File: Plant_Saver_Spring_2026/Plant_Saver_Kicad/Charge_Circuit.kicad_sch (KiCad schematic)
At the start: 23 parts, among them J1 1.25mm, Q1 ISP12DP06NMXTSA1, Q2 G09P02L, Q3 G09P02L, Q4 G09P02L, Q5 G09P02L, Q6 G09P02L, Q7 G09P02L, Q8 G09P02L, SW7 SA72SB0, U10 DW03C, U11 CDBA140SL-HF, U12 CDBA140SL-HF

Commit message: Found NTC Thermistor
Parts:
- R4, R5: value Therm -> NTCLE317E4103SBA
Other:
- moved on the sheet: BT1, C3, J1, Q1, Q2, Q3, Q4, Q5, Q6, Q7, Q8, R2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

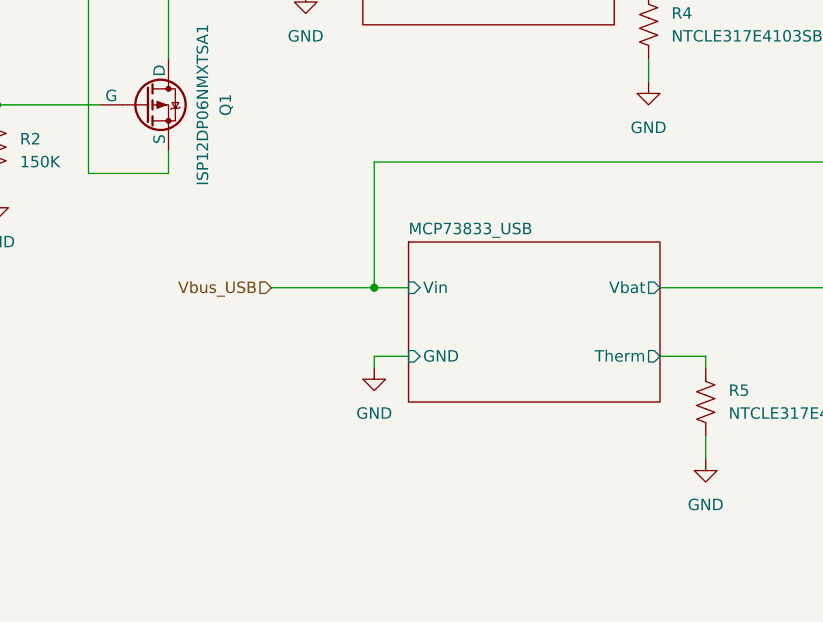
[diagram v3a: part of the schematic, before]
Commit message: Footprint updates
Misc. schematic fixes, mostly updated/added footprints where needed.
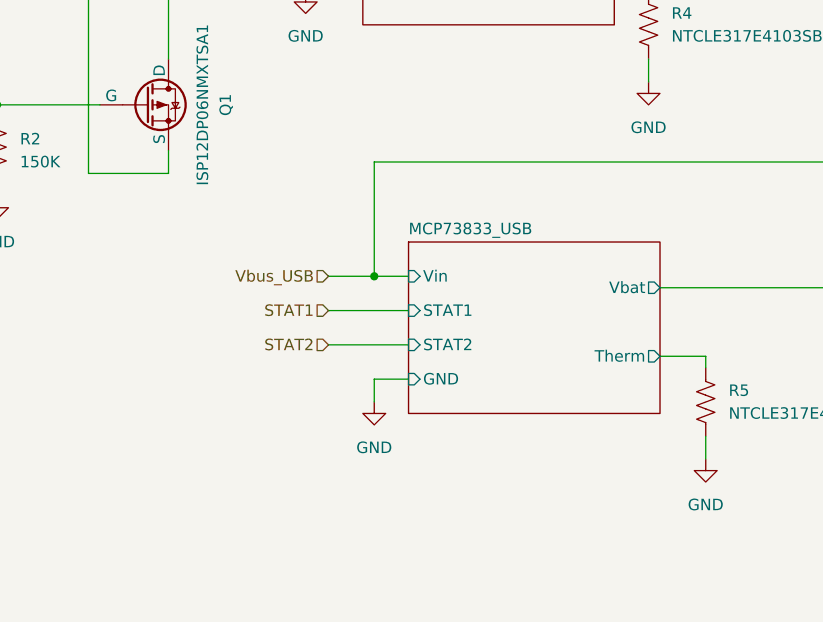
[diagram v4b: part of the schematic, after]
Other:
- sheet MCP73833_USB ports: added STAT1, STAT2; removed none
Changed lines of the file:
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@@
 	)
 	(junction
-		(at 113.03 87.63)
-		(diameter 0)
-		(color 0 0 0 0)
-	)
-	(junction
 		(at 166.37 73.66)
 		(diameter 0)
@@
 	)
 	(junction
+		(at 113.03 86.36)
+		(diameter 0)
+		(color 0 0 0 0)
+	)
+	(junction
 		(at 172.72 54.61)
 		(diameter 0)
@@
 	(wire
 		(pts
-			(xy 116.84 95.25) (xy 113.03 95.25)
+			(xy 113.03 86.36) (xy 116.84 86.36)
 		)
 		(stroke
@@
 	(wire
 		(pts
-			(xy 113.03 87.63) (xy 116.84 87.63)
+			(xy 139.7 45.72) (xy 154.94 45.72)
 		)
 		(stroke
@@
 	(wire
 		(pts
-			(xy 139.7 45.72) (xy 154.94 45.72)
+			(xy 107.95 86.36) (xy 113.03 86.36)
 		)
 		(stroke
@@
 	(wire
 		(pts
-			(xy 101.6 87.63) (xy 113.03 87.63)
+			(xy 39.37 50.8) (xy 39.37 52.07)
 		)
 		(stroke
@@
 	(wire
 		(pts
-			(xy 39.37 50.8) (xy 39.37 52.07)
+			(xy 238.76 95.25) (xy 234.95 95.25)
 		)
 		(stroke
@@
 	(wire
 		(pts
-			(xy 238.76 95.25) (xy 234.95 95.25)
+			(xy 201.93 78.74) (xy 203.2 78.74)
 		)
 		(stroke
@@
 	(wire
 		(pts
-			(xy 201.93 78.74) (xy 203.2 78.74)
+			(xy 210.82 80.01) (xy 210.82 78.74)
 		)
 		(stroke
@@
 	(wire
 		(pts
-			(xy 210.82 80.01) (xy 210.82 78.74)
+			(xy 166.37 73.66) (xy 166.37 54.61)
 		)
 		(stroke
@@
 	(wire
 		(pts
-			(xy 166.37 73.66) (xy 166.37 54.61)
+			(xy 107.95 93.98) (xy 116.84 93.98)
 		)
 		(stroke
@@
 	(wire
 		(pts
-			(xy 113.03 95.25) (xy 113.03 96.52)
+			(xy 107.95 45.72) (xy 107.95 35.56)
 		)
 		(stroke
@@
 	(wire
 		(pts
-			(xy 107.95 45.72) (xy 107.95 35.56)
+			(xy 143.51 62.23) (xy 143.51 64.77)
 		)
 		(stroke
@@
 	(wire
 		(pts
-			(xy 143.51 62.23) (xy 143.51 64.77)
+			(xy 213.36 60.96) (xy 218.44 60.96)
 		)
 		(stroke
@@
 	(wire
 		(pts
-			(xy 213.36 60.96) (xy 218.44 60.96)
+			(xy 113.03 97.79) (xy 113.03 100.33)
 		)
 		(stroke
@@
 	(wire
 		(pts
-			(xy 113.03 87.63) (xy 113.03 73.66)
+			(xy 185.42 43.18) (xy 185.42 44.45)
 		)
 		(stroke
@@
 	(wire
 		(pts
-			(xy 185.42 43.18) (xy 185.42 44.45)
+			(xy 210.82 132.08) (xy 210.82 135.89)
 		)
 		(stroke
@@
 	(wire
 		(pts
-			(xy 210.82 132.08) (xy 210.82 135.89)
+			(xy 113.03 86.36) (xy 113.03 73.66)
 		)
 		(stroke
@@
 	(wire
 		(pts
+			(xy 107.95 90.17) (xy 116.84 90.17)
+		)
+		(stroke
+			(width 0)
+			(type default)
+		)
+	)
+	(wire
+		(pts
 			(xy 223.52 60.96) (xy 218.44 60.96)
 		)
@@
 	(wire
 		(pts
+			(xy 113.03 97.79) (xy 116.84 97.79)
+		)
+		(stroke
+			(width 0)
+			(type default)
+		)
+	)
+	(wire
+		(pts
 			(xy 210.82 135.89) (xy 207.01 135.89)
 		)
@@
 		)
 	)
+	(hierarchical_label "STAT2"
+		(shape input)
+		(at 107.95 93.98 180)
+		(effects
+			(font
+				(size 1.27 1.27)
+			)
+			(justify right)
+		)
+	)
+	(hierarchical_label "STAT1"
+		(shape input)
+		(at 107.95 90.17 180)
+		(effects
+			(font
+				(size 1.27 1.27)
+			)
+			(justify right)
+		)
+	)
 	(hierarchical_label "3V3"
 		(shape input)
@@
 	(hierarchical_label "Vbus_USB"
 		(shape input)
-		(at 101.6 87.63 180)
+		(at 107.95 86.36 180)
 		(effects
 			(font
@@
 	(symbol
 		(lib_id "power:GND")
-		(at 113.03 96.52 0)
+		(at 113.03 100.33 0)
 		(unit 1)
 		(exclude_from_sim no)
@@
 		(fields_autoplaced yes)
 		(property "Reference" "#PWR016"
-			(at 113.03 102.87 0)
+			(at 113.03 106.68 0)
 			(effects
 				(font
@@
 		)
 		(property "Value" "GND"
-			(at 113.03 101.6 0)
+			(at 113.03 105.41 0)
 			(effects
 				(font
@@
 		)
 		(property "Footprint" ""
-			(at 113.03 96.52 0)
+			(at 113.03 100.33 0)
 			(effects
 				(font
@@
 		)
 		(property "Datasheet" ""
-			(at 113.03 96.52 0)
+			(at 113.03 100.33 0)
 			(effects
 				(font
@@
 		)
 		(property "Description" "Power symbol creates a global label with name \"GND\" , ground"
-			(at 113.03 96.52 0)
+			(at 113.03 100.33 0)
 			(effects
 				(font
@@
 	(sheet
 		(at 116.84 82.55)
-		(size 27.94 17.78)
+		(size 27.94 19.05)
 		(exclude_from_sim no)
 		(in_bom yes)
@@
 		)
 		(property "Sheetfile" "MCP73833_USB.kicad_sch"
-			(at 116.84 100.9146 0)
+			(at 116.84 102.1846 0)
 			(effects
 				(font
@@
 		)
 		(pin "GND" input
-			(at 116.84 95.25 180)
+			(at 116.84 97.79 180)
 			(effects
 				(font
@@
 		)
 		(pin "Vin" input
-			(at 116.84 87.63 180)
+			(at 116.84 86.36 180)
+			(effects
+				(font
+					(size 1.27 1.27)
+				)
+				(justify left)
+			)
+		)
+		(pin "STAT1" input
+			(at 116.84 90.17 180)
+			(effects
+				(font
+					(size 1.27 1.27)
+				)
+				(justify left)
+			)
+		)
+		(pin "STAT2" input
+			(at 116.84 93.98 180)
 			(effects
 				(font

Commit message: Started PCB
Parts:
- added TP10, TP8, TP9: TestPoint, TestPoint:TestPoint_Pad_1.5x1.5mm, symbol Connector:TestPoint
- U10: footprint (none) -> Package_TO_SOT_SMD:SOT-23-5_HandSoldering
- U11: renamed from U12; footprint (none) -> CDBA140SL_HF:CDBA-HF
- U9: renamed from U11; footprint (none) -> CDBA140SL_HF:CDBA-HF
- renumbered C3 to C5, J1 to J9, Q8 to Q10, Q1 to Q3, Q2 to Q4, Q3 to Q5, Q4 to Q6, Q5 to Q7, Q6 to Q8, Q7 to Q9, R5 to R10, R6 to R11, R8 to R12, R9 to R13, R7 to R14, R2 to R7, R3 to R8, R4 to R9, SW7 to SW4
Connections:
- net MCP73833_Solar/Vin: now also TP8.1
- net MCP73833_USB/Vbat: now also TP9.1
- net Vout: now also TP10.1

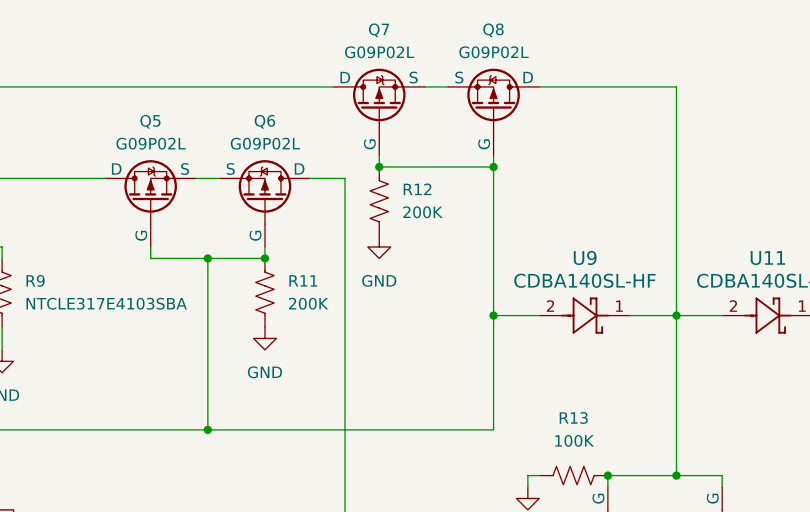
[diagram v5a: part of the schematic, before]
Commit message: Refined PCB layout
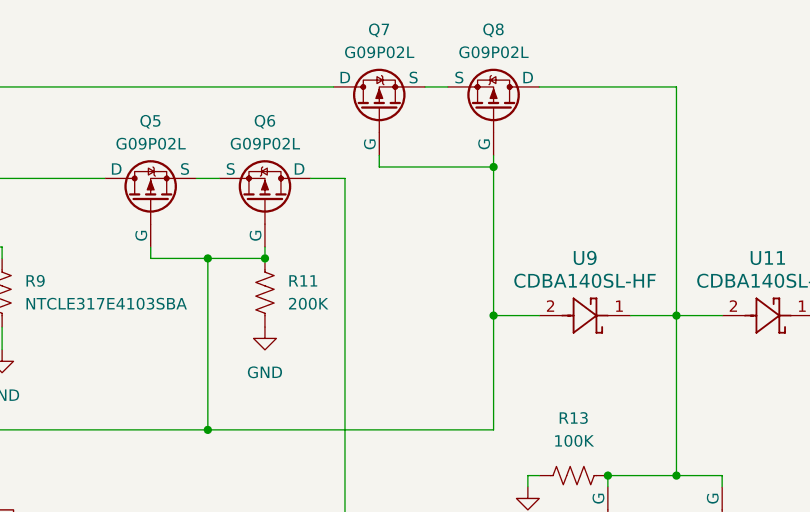
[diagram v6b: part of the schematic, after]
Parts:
- removed R12: 200K, Resistor_THT:R_Axial_DIN0207_L6.3mm_D2.5mm_P10.16mm_Horizontal, symbol Device:R_US
- C5: footprint C410C105K5R5TA7200:CAP_C410C_AX_X7R_AXIMAX_KEM -> Capacitor_SMD:C_1206_3216Metric_Pad1.33x1.80mm_HandSolder
- R11, R13, R14, R7, R8: footprint Resistor_THT:R_Axial_DIN0207_L6.3mm_D2.5mm_P10.16mm_Horizontal -> Resistor_SMD:R_1206_3216Metric_Pad1.30x1.75mm_HandSolder
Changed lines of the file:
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@@
 	)
 	(junction
-		(at 185.42 44.45)
-		(diameter 0)
-		(color 0 0 0 0)
-	)
-	(junction
 		(at 210.82 116.84)
 		(diameter 0)
@@
 	(symbol
 		(lib_id "Device:R_US")
-		(at 185.42 48.26 180)
-		(unit 1)
-		(exclude_from_sim no)
-		(in_bom yes)
-		(on_board yes)
-		(dnp no)
-		(fields_autoplaced yes)
-		(property "Reference" "R12"
-			(at 187.96 46.9899 0)
-			(effects
-				(font
-					(size 1.27 1.27)
-				)
-				(justify right)
-			)
-		)
-		(property "Value" "200K"
-			(at 187.96 49.5299 0)
-			(effects
-				(font
-					(size 1.27 1.27)
-				)
-				(justify right)
-			)
-		)
-		(property "Footprint" "Resistor_THT:R_Axial_DIN0207_L6.3mm_D2.5mm_P10.16mm_Horizontal"
-			(at 184.404 48.006 90)
-			(effects
-				(font
-					(size 1.27 1.27)
-				)
-				(hide yes)
-			)
-		)
-		(property "Datasheet" "~"
-			(at 185.42 48.26 0)
-			(effects
-				(font
-					(size 1.27 1.27)
-				)
-				(hide yes)
-			)
-		)
-		(property "Description" "Resistor, US symbol"
-			(at 185.42 48.26 0)
-			(effects
-				(font
-					(size 1.27 1.27)
-				)
-				(hide yes)
-			)
-		)
-		(pin "2"
-		)
-		(pin "1"
-		)
-		(instances
-			(project "Plant_Saver_Dev"
-				(path "/681e180a-075d-4ade-9671-1538248e0c71/5dcd62e6-4375-4774-94ca-6833cc877f09"
-					(reference "R15")
-					(unit 1)
-				)
-			)
-			(project "Charge_Circuit"
-				(path "/6972ab9f-ec90-4565-bd2c-bfb60d5a21f0"
-					(reference "R7")
-					(unit 1)
-				)
-			)
-			(project "Plant_Saver_Dev"
-				(path "/7f244634-d37a-4ff0-ba36-8027330ab1bd/c1b5c94f-5fb5-4e2b-895b-5d171c372d7d"
-					(reference "R12")
-					(unit 1)
-				)
-			)
-		)
-	)
-	(symbol
-		(lib_id "Device:R_US")
 		(at 172.72 58.42 180)
 		(unit 1)
@@
 			)
 		)
-		(property "Footprint" "Resistor_THT:R_Axial_DIN0207_L6.3mm_D2.5mm_P10.16mm_Horizontal"
+		(property "Footprint" "Resistor_SMD:R_1206_3216Metric_Pad1.30x1.75mm_HandSolder"
 			(at 171.704 58.166 90)
 			(effects
@@
 			)
 		)
-		(property "Footprint" "Resistor_THT:R_Axial_DIN0207_L6.3mm_D2.5mm_P10.16mm_Horizontal"
+		(property "Footprint" "Resistor_SMD:R_1206_3216Metric_Pad1.30x1.75mm_HandSolder"
 			(at 70.104 72.136 90)
 			(effects
@@
 			)
 		)
-		(property "Footprint" "Resistor_THT:R_Axial_DIN0207_L6.3mm_D2.5mm_P10.16mm_Horizontal"
+		(property "Footprint" "Resistor_SMD:R_1206_3216Metric_Pad1.30x1.75mm_HandSolder"
 			(at 206.756 79.756 90)
 			(effects
@@
 			)
 		)
-		(property "Footprint" "Resistor_THT:R_Axial_DIN0207_L6.3mm_D2.5mm_P10.16mm_Horizontal"
+		(property "Footprint" "Resistor_SMD:R_1206_3216Metric_Pad1.30x1.75mm_HandSolder"
 			(at 207.264 105.664 90)
 			(effects
@@
 			)
 		)
-		(property "Footprint" "C410C105K5R5TA7200:CAP_C410C_AX_X7R_AXIMAX_KEM"
+		(property "Footprint" "Capacitor_SMD:C_1206_3216Metric_Pad1.33x1.80mm_HandSolder"
 			(at 209.55 115.8748 0)
 			(effects
@@
 			)
 		)
-		(property "Footprint" "Resistor_THT:R_Axial_DIN0207_L6.3mm_D2.5mm_P10.16mm_Horizontal"
+		(property "Footprint" "Resistor_SMD:R_1206_3216Metric_Pad1.30x1.75mm_HandSolder"
 			(at 98.044 52.324 90)
 			(effects
@@
 					(unit 1)
 				)
-			)
-		)
-	)
-	(symbol
-		(lib_id "power:GND")
-		(at 185.42 52.07 0)
-		(unit 1)
-		(exclude_from_sim no)
-		(in_bom yes)
-		(on_board yes)
-		(dnp no)
-		(fields_autoplaced yes)
-		(property "Reference" "#PWR022"
-			(at 185.42 58.42 0)
-			(effects
-				(font
-					(size 1.27 1.27)
-				)
-				(hide yes)
-			)
-		)
-		(property "Value" "GND"
-			(at 185.42 57.15 0)
-			(effects
-				(font
-					(size 1.27 1.27)
-				)
-			)
-		)
-		(property "Footprint" ""
-			(at 185.42 52.07 0)
-			(effects
-				(font
-					(size 1.27 1.27)
-				)
-				(hide yes)
-			)
-		)
-		(property "Datasheet" ""
-			(at 185.42 52.07 0)
-			(effects
-				(font
-					(size 1.27 1.27)
-				)
-				(hide yes)
-			)
-		)
-		(property "Description" "Power symbol creates a global label with name \"GND\" , ground"
-			(at 185.42 52.07 0)
-			(effects
-				(font
-					(size 1.27 1.27)
-				)
-				(hide yes)
-			)
-		)
-		(pin "1"
-		)
-		(instances
-			(project "Plant_Saver_Dev"
-				(path "/681e180a-075d-4ade-9671-1538248e0c71/5dcd62e6-4375-4774-94ca-6833cc877f09"
-					(reference "#PWR04")
-					(unit 1)
-				)
-			)
-			(project "Charge_Circuit"
-				(path "/6972ab9f-ec90-4565-bd2c-bfb60d5a21f0"
-					(reference "#PWR09")
-					(unit 1)
-				)
-			)
-			(project "Plant_Saver_Dev"
-				(path "/7f244634-d37a-4ff0-ba36-8027330ab1bd/c1b5c94f-5fb5-4e2b-895b-5d171c372d7d"
-					(reference "#PWR022")
-					(unit 1)
-				)

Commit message: PCB Routing
I believe this to be the product of mania, but it may yet function.
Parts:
- TP8: footprint TestPoint:TestPoint_Pad_1.5x1.5mm -> TestPoint:TestPoint_Pad_1.0x1.0mm
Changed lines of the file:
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@@
 			)
 		)
-		(property "Footprint" "TestPoint:TestPoint_Pad_1.5x1.5mm"
+		(property "Footprint" "TestPoint:TestPoint_Pad_1.0x1.0mm"
 			(at 104.14 63.5 0)
 			(effects

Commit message: PCB Pre-Check complete
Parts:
- renumbered TP9 to BAT1, TP10 to BUS1, J9 to J10, R8 to R10, R9 to R11, R10 to R12, R11 to R13, R13 to R14, R14 to R15, R7 to R9, TP8 to SOLB1
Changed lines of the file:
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@@
 		(dnp no)
 		(fields_autoplaced yes)
-		(property "Reference" "R11"
+		(property "Reference" "R13"
 			(at 175.26 57.1499 0)
 			(effects
@@
 			(project "Plant_Saver_Dev"
 				(path "/7f244634-d37a-4ff0-ba36-8027330ab1bd/c1b5c94f-5fb5-4e2b-895b-5d171c372d7d"
-					(reference "R11")
+					(reference "R13")
 					(unit 1)
 				)
@@
 		(dnp no)
 		(fields_autoplaced yes)
-		(property "Reference" "TP9"
+		(property "Reference" "BAT1"
 			(at 184.15 94.7419 0)
 			(effects
@@
 			(project "Plant_Saver_Kicad"
 				(path "/7f244634-d37a-4ff0-ba36-8027330ab1bd/c1b5c94f-5fb5-4e2b-895b-5d171c372d7d"
-					(reference "TP9")
+					(reference "BAT1")
 					(unit 1)
 				)
@@
 		(on_board yes)
 		(dnp no)
-		(property "Reference" "J9"
+		(property "Reference" "J10"
 			(at 200.66 143.5099 90)
 			(effects
@@
 			(project ""
 				(path "/7f244634-d37a-4ff0-ba36-8027330ab1bd/c1b5c94f-5fb5-4e2b-895b-5d171c372d7d"
-					(reference "J9")
+					(reference "J10")
 					(unit 1)
 				)
@@
 		(dnp no)
 		(fields_autoplaced yes)
-		(property "Reference" "#PWR018"
+		(property "Reference" "#PWR019"
 			(at 113.03 106.68 0)
 			(effects
@@
 			(project "Plant_Saver_Dev"
 				(path "/7f244634-d37a-4ff0-ba36-8027330ab1bd/c1b5c94f-5fb5-4e2b-895b-5d171c372d7d"
-					(reference "#PWR018")
+					(reference "#PWR019")
 					(unit 1)
 				)
@@
 		(dnp no)
 		(fields_autoplaced yes)
-		(property "Reference" "R7"
+		(property "Reference" "R9"
 			(at 73.66 71.1199 0)
 			(effects
@@
 			(project "Plant_Saver_Dev"
 				(path "/7f244634-d37a-4ff0-ba36-8027330ab1bd/c1b5c94f-5fb5-4e2b-895b-5d171c372d7d"
-					(reference "R7")
+					(reference "R9")
 					(unit 1)
 				)
@@
 		(dnp no)
 		(fields_autoplaced yes)
-		(property "Reference" "R13"
+		(property "Reference" "R14"
 			(at 207.01 72.39 90)
 			(effects
@@
 			(project "Plant_Saver_Dev"
 				(path "/7f244634-d37a-4ff0-ba36-8027330ab1bd/c1b5c94f-5fb5-4e2b-895b-5d171c372d7d"
-					(reference "R13")
+					(reference "R14")
 					(unit 1)
 				)
@@
 		(dnp no)
 		(fields_autoplaced yes)
-		(property "Reference" "R14"
+		(property "Reference" "R15"
 			(at 207.01 100.33 90)
 			(effects
@@
 			(project "Plant_Saver_Kicad"
 				(path "/7f244634-d37a-4ff0-ba36-8027330ab1bd/c1b5c94f-5fb5-4e2b-895b-5d171c372d7d"
-					(reference "R14")
+					(reference "R15")
 					(unit 1)
 				)
@@
 		(on_board yes)
 		(dnp no)
-		(property "Reference" "#PWR019"
+		(property "Reference" "#PWR020"
 			(at 143.51 71.12 0)
 			(effects
@@
 			(project "Plant_Saver_Kicad"
 				(path "/7f244634-d37a-4ff0-ba36-8027330ab1bd/c1b5c94f-5fb5-4e2b-895b-5d171c372d7d"
-					(reference "#PWR019")
+					(reference "#PWR020")
 					(unit 1)
 				)
@@
 		(dnp no)
 		(fields_autoplaced yes)
-		(property "Reference" "#PWR017"
+		(property "Reference" "#PWR018"
 			(at 105.41 60.96 0)
 			(effects
@@
 			(project "Plant_Saver_Dev"
 				(path "/7f244634-d37a-4ff0-ba36-8027330ab1bd/c1b5c94f-5fb5-4e2b-895b-5d171c372d7d"
-					(reference "#PWR017")
+					(reference "#PWR018")
 					(unit 1)
 				)
@@
 		(dnp no)
 		(fields_autoplaced yes)
-		(property "Reference" "R9"
+		(property "Reference" "R11"
 			(at 146.05 57.1499 0)
 			(effects
@@
 			(project "Plant_Saver_Kicad"
 				(path "/7f244634-d37a-4ff0-ba36-8027330ab1bd/c1b5c94f-5fb5-4e2b-895b-5d171c372d7d"
-					(reference "R9")
+					(reference "R11")
 					(unit 1)
 				)
@@
 		(dnp no)
 		(fields_autoplaced yes)
-		(property "Reference" "#PWR021"
+		(property "Reference" "#PWR022"
 			(at 172.72 68.58 0)
 			(effects
@@
 			(project "Plant_Saver_Dev"
 				(path "/7f244634-d37a-4ff0-ba36-8027330ab1bd/c1b5c94f-5fb5-4e2b-895b-5d171c372d7d"
-					(reference "#PWR021")
+					(reference "#PWR022")
 					(unit 1)
 				)
@@
 		(on_board yes)
 		(dnp no)
-		(property "Reference" "#PWR016"
+		(property "Reference" "#PWR017"
 			(at 71.12 83.82 0)
 			(effects
@@
 			(project "Plant_Saver_Dev"
 				(path "/7f244634-d37a-4ff0-ba36-8027330ab1bd/c1b5c94f-5fb5-4e2b-895b-5d171c372d7d"
-					(reference "#PWR016")
+					(reference "#PWR017")
 					(unit 1)
 				)
@@
 		(dnp no)
 		(fields_autoplaced yes)
-		(property "Reference" "#PWR020"
+		(property "Reference" "#PWR021"
 			(at 149.86 113.03 0)
 			(effects
@@
 			(project "Plant_Saver_Kicad"
 				(path "/7f244634-d37a-4ff0-ba36-8027330ab1bd/c1b5c94f-5fb5-4e2b-895b-5d171c372d7d"
-					(reference "#PWR020")
+					(reference "#PWR021")
 					(unit 1)
 				)
@@
 		(dnp no)
 		(fields_autoplaced yes)
-		(property "Reference" "#PWR015"
+		(property "Reference" "#PWR016"
 			(at 39.37 58.42 0)
 			(effects
@@
 			(project "Plant_Saver_Dev"
 				(path "/7f244634-d37a-4ff0-ba36-8027330ab1bd/c1b5c94f-5fb5-4e2b-895b-5d171c372d7d"
-					(reference "#PWR015")
+					(reference "#PWR016")
 					(unit 1)
 				)
@@
 		(dnp no)
 		(fields_autoplaced yes)
-		(property "Reference" "TP8"
+		(property "Reference" "SOLB1"
 			(at 111.76 65.5319 0)
 			(effects
@@
 			(project "Plant_Saver_Kicad"
 				(path "/7f244634-d37a-4ff0-ba36-8027330ab1bd/c1b5c94f-5fb5-4e2b-895b-5d171c372d7d"
-					(reference "TP8")
+					(reference "SOLB1")
 					(unit 1)
 				)
@@
 		(dnp no)
 		(fields_autoplaced yes)
-		(property "Reference" "R8"
+		(property "Reference" "R10"
 			(at 97.79 46.99 90)
 			(effects
@@
 			(project ""
 				(path "/7f244634-d37a-4ff0-ba36-8027330ab1bd/c1b5c94f-5fb5-4e2b-895b-5d171c372d7d"
-					(reference "R8")
+					(reference "R10")
 					(unit 1)
 				)
@@
 		(dnp no)
 		(fields_autoplaced yes)
-		(property "Reference" "TP10"
+		(property "Reference" "BUS1"
 			(at 270.51 99.8219 0)
 			(effects
@@
 			(project "Plant_Saver_Kicad"
 				(path "/7f244634-d37a-4ff0-ba36-8027330ab1bd/c1b5c94f-5fb5-4e2b-895b-5d171c372d7d"
-					(reference "TP10")
+					(reference "BUS1")
 					(unit 1)
 				)
@@
 		(dnp no)
 		(fields_autoplaced yes)
-		(property "Reference" "R10"
+		(property "Reference" "R12"
 			(at 152.4 99.0599 0)
 			(effects
@@
 			(project "Plant_Saver_Kicad"
 				(path "/7f244634-d37a-4ff0-ba36-8027330ab1bd/c1b5c94f-5fb5-4e2b-895b-5d171c372d7d"
-					(reference "R10")
-					(unit 1)
-				)
+					(reference "R12")
+					(unit 1)
+				)
